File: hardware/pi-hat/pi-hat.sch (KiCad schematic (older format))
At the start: 81 parts, among them J1 PWR IN, J10 6-8, J11 PWM0, J12 PWM1, J13 KLPX-0848A-2-B, J14 KLPX-0848A-2-R, J2 A-F, J3 40HAT, J4 G-M, J5 N-Q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

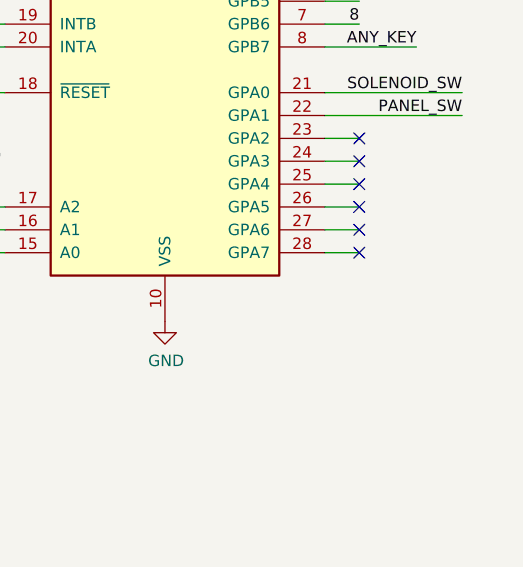
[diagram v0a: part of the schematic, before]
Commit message: add indicator led
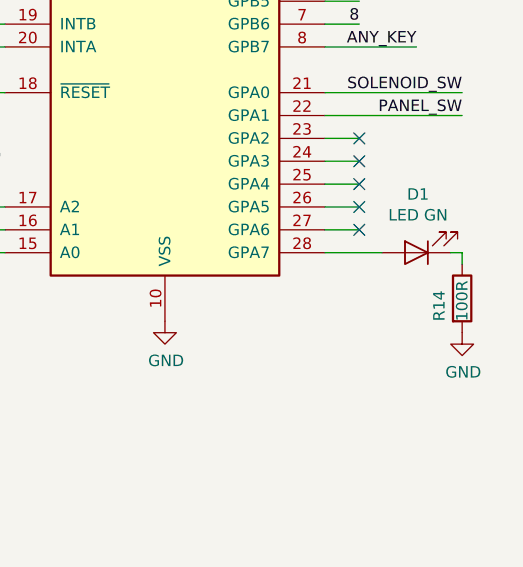
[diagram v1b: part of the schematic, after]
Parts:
- added D1: LED GN, LED_SMD:LED_0603_1608Metric, symbol Device:LED
- added R14: 100R, symbol Device:R
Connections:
- net GND: now also R14.2
- net at U9.28 (GPA7): now also D1.2 (A)
- new net: D1.1 (K), R14.1
- no-connect marks 31 -> 30
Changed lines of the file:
@@
 Wire Wire Line
 	15200 9150 15350 9150
-Wire Wire Line
-	15200 9250 15350 9250
 NoConn ~ 15350 8750
 NoConn ~ 15350 8850
@@
 NoConn ~ 15350 9050
 NoConn ~ 15350 9150
-NoConn ~ 15350 9250
 Wire Wire Line
 	13800 8250 13750 8250
@@
 Wire Wire Line
 	5750 2750 5750 2600
+$Comp
+L Device:LED D1
+U 1 1 5EC5AE89
+P 15600 9250
+F 0 "D1" H 15593 8995 50  0000 C CNN
+F 1 "LED GN" H 15593 9086 50  0000 C CNN
+F 2 "LED_SMD:LED_0603_1608Metric" H 15600 9250 50  0001 C CNN
+F 3 "~" H 15600 9250 50  0001 C CNN
+	1    15600 9250
+	-1   0    0    1
+$EndComp
+$Comp
+L power:GND #PWR0122
+U 1 1 5EC5E7A0
+P 15800 9600
+F 0 "#PWR0122" H 15800 9350 50  0001 C CNN
+F 1 "GND" H 15805 9427 50  0000 C CNN
+F 2 "" H 15800 9600 50  0001 C CNN
+F 3 "" H 15800 9600 50  0001 C CNN
+	1    15800 9600
+	1    0    0    -1
+$EndComp
+Wire Wire Line
+	15200 9250 15450 9250
+Wire Wire Line
+	15750 9250 15800 9250
+Wire Wire Line
+	15800 9250 15800 9300
+$Comp
+L Device:R R14
+U 1 1 5EC5DD42
+P 15800 9450
+F 0 "R14" V 15700 9350 50  0000 L CNN
+F 1 "100R" V 15800 9350 50  0000 L CNN
+F 2 "" V 15730 9450 50  0001 C CNN
+F 3 "~" H 15800 9450 50  0001 C CNN
+	1    15800 9450
+	1    0    0    -1
+$EndComp
 $EndSCHEMATC

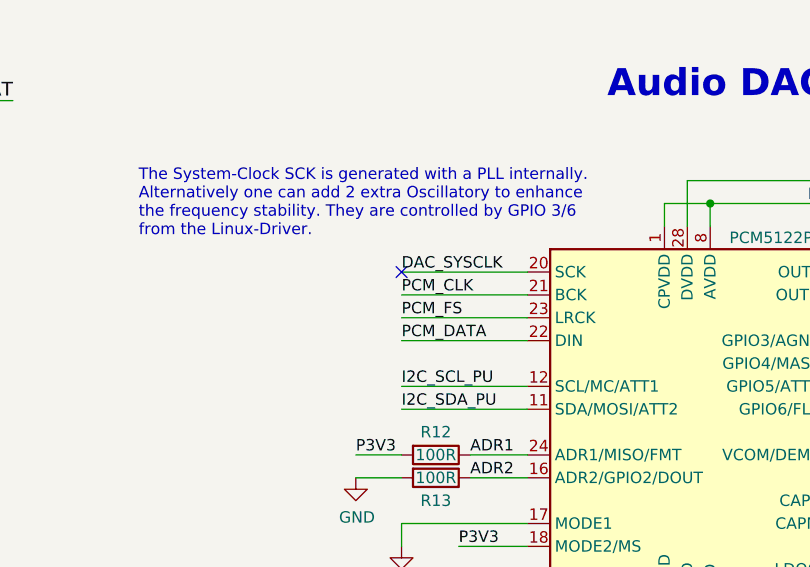
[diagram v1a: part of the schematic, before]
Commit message: add jumper to optionally bridge pcm_clk and sclk as per datasheet
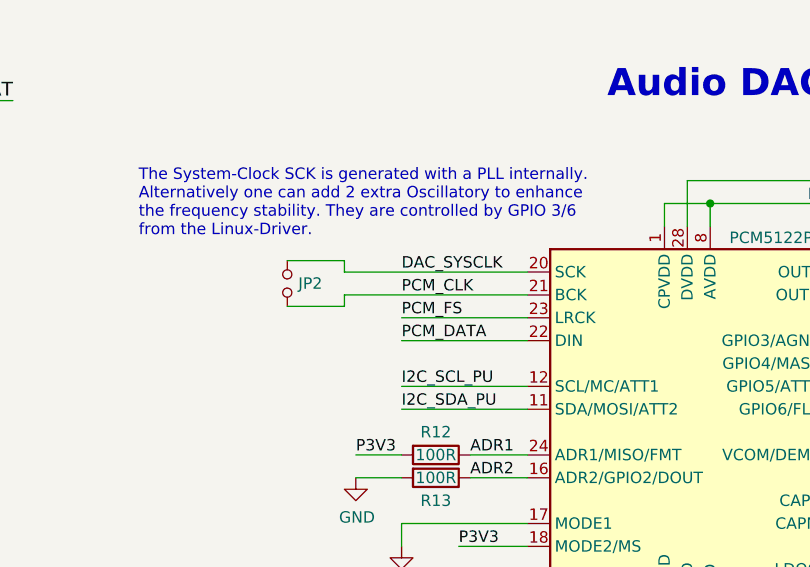
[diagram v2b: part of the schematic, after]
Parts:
- added JP2: Jumper_NO_Small, Jumper:SolderJumper-2_P1.3mm_Open_Pad1.0x1.5mm, symbol Device:Jumper_NO_Small
- R14: footprint (none) -> Resistor_SMD:R_0805_2012Metric
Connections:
- net DAC_SYSCLK: now also JP2.1
- net PCM_CLK: now also JP2.2
- no-connect marks 30 -> 29
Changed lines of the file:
@@
 Text Label 4700 7950 0    50   ~ 0
 PCM_FS
-Wire Wire Line
-	5250 7850 4700 7850
 Text Label 4700 7850 0    50   ~ 0
 PCM_CLK
-Wire Wire Line
-	5250 7750 4700 7750
-NoConn ~ 4700 7750
 NoConn ~ 6650 8050
 NoConn ~ 6650 8150
@@
 F 0 "R14" V 15700 9350 50  0000 L CNN
 F 1 "100R" V 15800 9350 50  0000 L CNN
-F 2 "" V 15730 9450 50  0001 C CNN
+F 2 "Resistor_SMD:R_0805_2012Metric" V 15730 9450 50  0001 C CNN
 F 3 "~" H 15800 9450 50  0001 C CNN
 	1    15800 9450
 	1    0    0    -1
 $EndComp
+$Comp
+L Device:Jumper_NO_Small JP2
+U 1 1 5DFD09F1
+P 4200 7800
+F 0 "JP2" V 4200 7848 50  0000 L CNN
+F 1 "Jumper_NO_Small" V 4245 7848 50  0001 L CNN
+F 2 "Jumper:SolderJumper-2_P1.3mm_Open_Pad1.0x1.5mm" H 4200 7800 50  0001 C CNN
+F 3 "~" H 4200 7800 50  0001 C CNN
+	1    4200 7800
+	0    1    1    0
+$EndComp
+Wire Wire Line
+	4450 7750 4450 7700
+Wire Wire Line
+	4450 7700 4200 7700
+Wire Wire Line
+	4450 7750 5250 7750
+Wire Wire Line
+	4200 7900 4450 7900
+Wire Wire Line
+	4450 7900 4450 7850
+Wire Wire Line
+	4450 7850 5250 7850
 $EndSCHEMATC

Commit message: final cleanup and order
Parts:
- R23, R29: value 10K -> 10k
- R24: value 47K -> 47k
- RN1, RN2, RN3, RN4, RN5, RN6: value EXB-38V103JV -> EXB-38V100JV
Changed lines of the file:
@@
 P 1400 6250
 F 0 "R29" V 1480 6250 50  0000 C CNN
-F 1 "10K" V 1400 6250 50  0000 C CNN
+F 1 "10k" V 1400 6250 50  0000 C CNN
 F 2 "Resistor_SMD:R_0805_2012Metric" V 1330 6250 50  0001 C CNN
 F 3 "" H 1400 6250 50  0001 C CNN
@@
 P 11900 5400
 F 0 "RN1" V 11600 5450 50  0000 R CNN
-F 1 "EXB-38V103JV" H 12100 5850 50  0000 R CNN
+F 1 "EXB-38V100JV" H 12100 5850 50  0000 R CNN
 F 2 "Resistor_SMD:R_Array_Convex_4x0603" V 12175 5400 50  0001 C CNN
 F 3 "~" H 11900 5400 50  0001 C CNN
@@
 P 12450 5400
 F 0 "RN2" V 12150 5450 50  0000 R CNN
-F 1 "EXB-38V103JV" H 12650 5950 50  0000 R CNN
+F 1 "EXB-38V100JV" H 12650 5950 50  0000 R CNN
 F 2 "Resistor_SMD:R_Array_Convex_4x0603" V 12725 5400 50  0001 C CNN
 F 3 "~" H 12450 5400 50  0001 C CNN
@@
 P 13000 5400
 F 0 "RN3" V 12700 5450 50  0000 R CNN
-F 1 "EXB-38V103JV" H 13250 5850 50  0000 R CNN
+F 1 "EXB-38V100JV" H 13250 5850 50  0000 R CNN
 F 2 "Resistor_SMD:R_Array_Convex_4x0603" V 13275 5400 50  0001 C CNN
 F 3 "~" H 13000 5400 50  0001 C CNN
@@
 P 13550 5400
 F 0 "RN4" V 13250 5450 50  0000 R CNN
-F 1 "EXB-38V103JV" H 13800 5950 50  0000 R CNN
+F 1 "EXB-38V100JV" H 13800 5950 50  0000 R CNN
 F 2 "Resistor_SMD:R_Array_Convex_4x0603" V 13825 5400 50  0001 C CNN
 F 3 "~" H 13550 5400 50  0001 C CNN
@@
 P 14100 5400
 F 0 "RN5" V 13800 5450 50  0000 R CNN
-F 1 "EXB-38V103JV" H 14350 5850 50  0000 R CNN
+F 1 "EXB-38V100JV" H 14350 5850 50  0000 R CNN
 F 2 "Resistor_SMD:R_Array_Convex_4x0603" V 14375 5400 50  0001 C CNN
 F 3 "~" H 14100 5400 50  0001 C CNN
@@
 P 14650 5400
 F 0 "RN6" V 14350 5450 50  0000 R CNN
-F 1 "EXB-38V103JV" H 14900 5950 50  0000 R CNN
+F 1 "EXB-38V100JV" H 14900 5950 50  0000 R CNN
 F 2 "Resistor_SMD:R_Array_Convex_4x0603" V 14925 5400 50  0001 C CNN
 F 3 "~" H 14650 5400 50  0001 C CNN
@@
 P 6550 3800
 F 0 "R24" V 6630 3800 50  0000 C CNN
-F 1 "47K" V 6550 3800 50  0000 C CNN
+F 1 "47k" V 6550 3800 50  0000 C CNN
 F 2 "Resistor_SMD:R_0805_2012Metric" V 6480 3800 50  0001 C CNN
 F 3 "" H 6550 3800 50  0001 C CNN
@@
 P 5750 3800
 F 0 "R23" V 5830 3800 50  0000 C CNN
-F 1 "10K" V 5750 3800 50  0000 C CNN
+F 1 "10k" V 5750 3800 50  0000 C CNN
 F 2 "Resistor_SMD:R_0805_2012Metric" V 5680 3800 50  0001 C CNN
 F 3 "" H 5750 3800 50  0001 C CNN

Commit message: change topology around Q4
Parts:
- added D2: ?, Diode_SMD:D_0805_2012Metric, symbol Device:D_Zener
- added Q5: DMN6075S, Package_TO_SOT_SMD:SOT-23, symbol Device:Q_NMOS_GSD
- added R15, R16: 10k, Resistor_SMD:R_0805_2012Metric, symbol Device:R
- Q4: value NTR4171P -> ?
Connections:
- net GND: now also U8.18 (~RESET~), Q5.2 (S), R15.1
- net P30V: now also Q4.2 (S), R4.2, D2.1 (K); no longer Q4.3 (D)
- net P3V3: no longer R4.2
- net PANEL_30V: now also Q4.3 (D); no longer Q4.2 (S)
- net at Q4.1 (G), R4.1: now also D2.2 (A), R16.2; no longer R3.1
- net LED: now reaches D1.2 (A), U9.28 (GPA7)
- new net: Q5.3 (D), R16.1
- new net: Q5.1 (G), R15.2, R3.1
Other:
- moved on the sheet: J7, Q3, Q4, R1, R2, R3, R4
